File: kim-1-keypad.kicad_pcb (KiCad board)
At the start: 2 copper layers, 89.4 x 48.7 mm, 41 parts, among them J1 Keyboard Connector, SW1 0, SW10 9, SW11 A, SW12 B, SW13 C, SW14 D, SW15 E, SW16 F, SW17 AD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

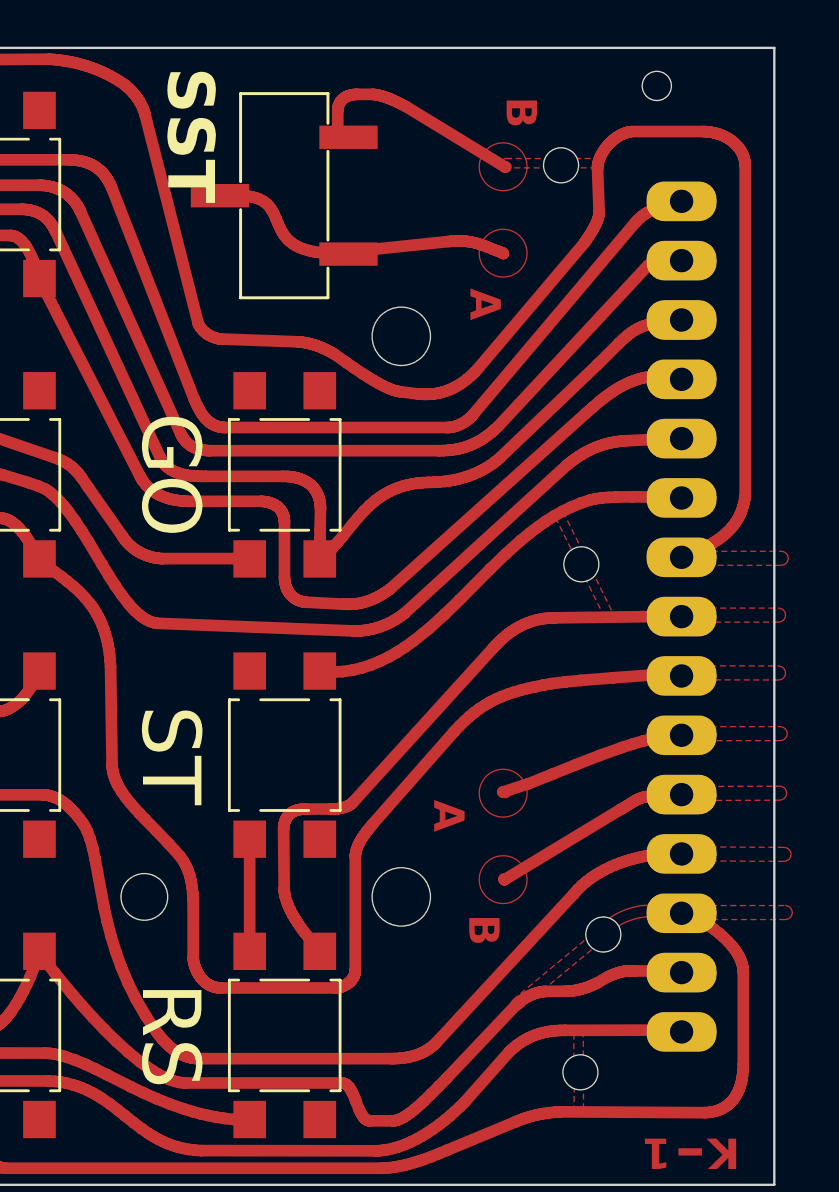
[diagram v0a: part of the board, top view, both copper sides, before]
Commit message: Fix silkscreen and connector pads
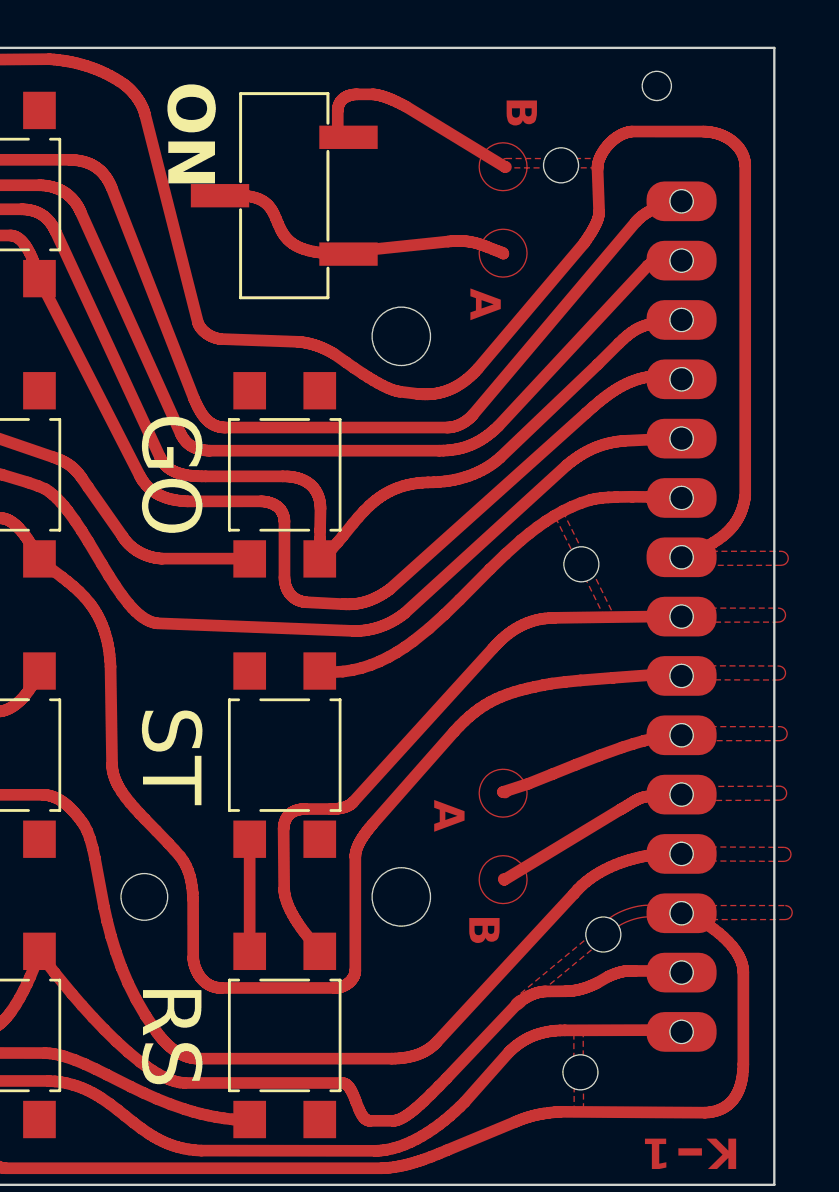
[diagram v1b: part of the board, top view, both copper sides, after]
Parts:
- J1: moved to F.Cu
- SW24: value SST -> ON
- turned J1 to 0 degrees
